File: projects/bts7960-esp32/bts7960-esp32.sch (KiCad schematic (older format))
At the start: 10 parts, among them J1 CONN_02X04, J2 CONN_01X04, U1 ESP32-DEVKIT-V1

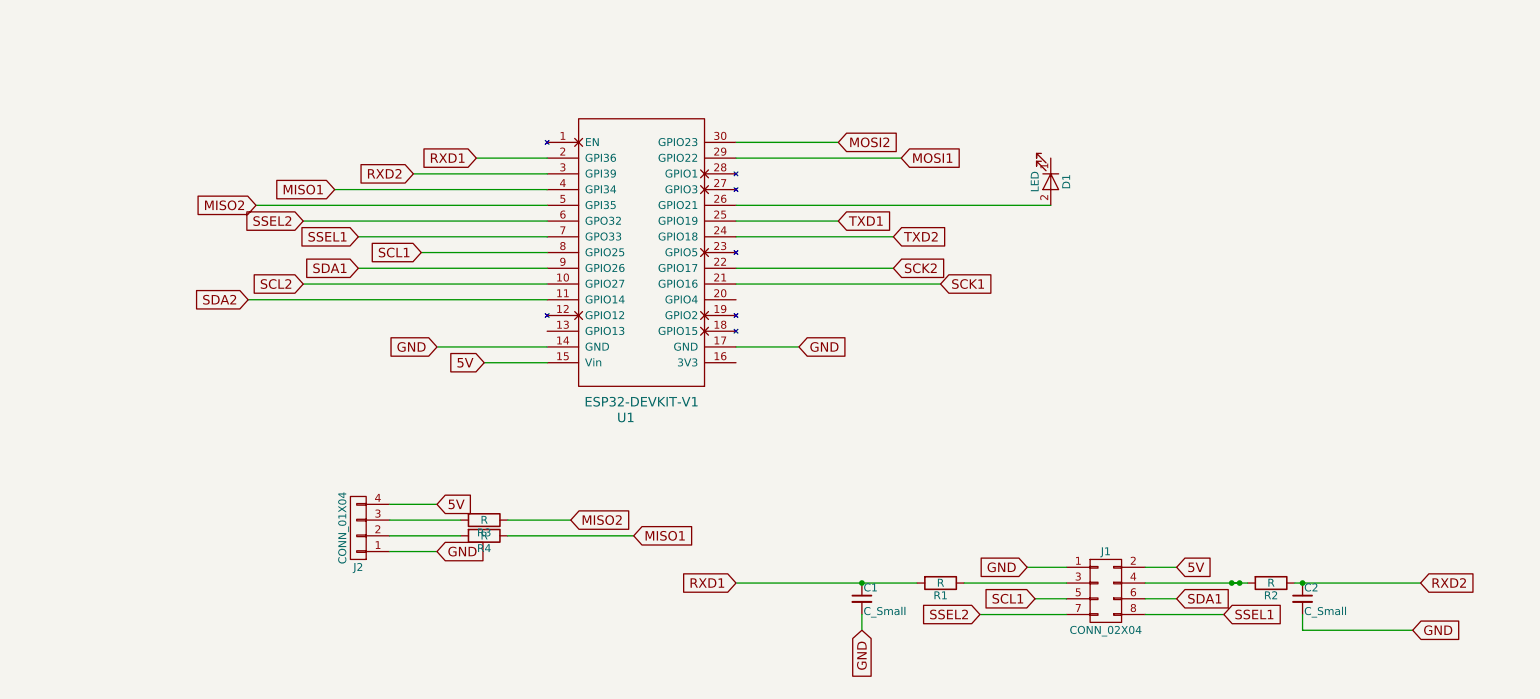
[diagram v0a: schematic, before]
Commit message: working on universal esp32 board
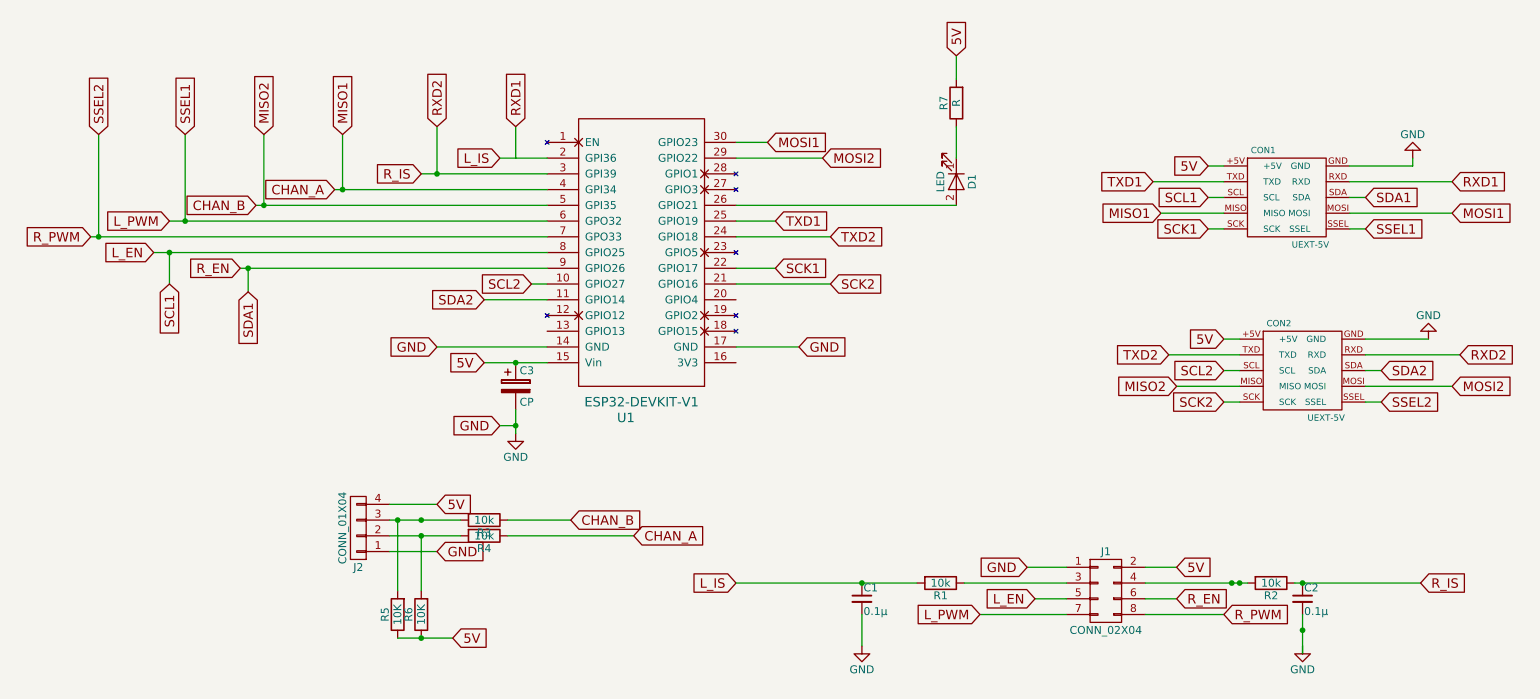
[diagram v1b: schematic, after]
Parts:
- added C3: CP, Capacitors_THT:CP_Radial_D6.3mm_P2.50mm, symbol CP
- added CON1, CON2: UEXT-5V, limero-lib:UEXT, symbol UEXT-5V
- added R5, R6: 10K, Resistors_THT:R_Axial_DIN0204_L3.6mm_D1.6mm_P5.08mm_Horizontal, symbol R
- added R7: R, Resistors_THT:R_Axial_DIN0204_L3.6mm_D1.6mm_P5.08mm_Horizontal, symbol R
- C1, C2: value C_Small -> 0.1µ
- D1: footprint LEDs:LED_Rectangular_W3.9mm_H1.9mm -> LEDs:LED_D5.0mm
- R1, R2: value R -> 10k; footprint Resistors_THT:R_Axial_DIN0204_L3.6mm_D1.6mm_P2.54mm_Vertical -> Resistors_THT:R_Axial_DIN0204_L3.6mm_D1.6mm_P5.08mm_Horizontal
- R3, R4: value R -> 10k
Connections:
- net 5V: now also C3.1, CON1.+5V, CON2.+5V, R5.1, R6.1, R7.2
- net GND: now also C3.2, CON1.GND, CON2.GND; no longer C2.2
- net MOSI1: now also U1.30 (GPIO23), CON1.MOSI; no longer U1.29 (GPIO22)
- net MOSI2: now also U1.29 (GPIO22), CON2.MOSI; no longer U1.30 (GPIO23)
- net RXD1: now also CON1.RXD; no longer C1.1, R1.2, U1.2 (GPI36)
- net RXD2: now also CON2.RXD
- net SCK1: now also U1.22 (GPIO17), CON1.SCK; no longer U1.21 (GPIO16)
- net SCK2: now also U1.21 (GPIO16), CON2.SCK; no longer U1.22 (GPIO17)
- net SCL2: now also CON2.SCL
- net SDA2: now also CON2.SDA
- net TXD1: now also CON1.TXD
- net TXD2: now also CON2.TXD
- net at D1.1 (K): now also R7.1
- net at J2.2 (P2), R4.2: now also R6.2
- net at J2.3 (P3), R3.2: now also R5.2
- net MISO1 renamed CHAN_A
- net CHAN_A: now also CON1.MISO
- net MISO2 renamed CHAN_B
- net CHAN_B: now also CON2.MISO
- net SCL1 renamed L_EN
- net L_EN: now also CON1.SCL
- net SDA1 renamed R_EN
- net R_EN: now also CON1.SDA
- net SSEL1 renamed R_PWM
- net R_PWM: now also CON2.SSEL
- net SSEL2 renamed L_PWM
- net L_PWM: now also CON1.SSEL
- new net L_IS: C1.1, R1.2, U1.2 (GPI36)
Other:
- moved on the sheet: D1
